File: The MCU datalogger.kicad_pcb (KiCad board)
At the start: 2 copper layers, 25 parts, among them J1 Conn_01x04_Male, J2 Conn_01x09_Male, J3 Conn_01x04_Male, J4 Conn_02x03_Odd_Even, U1 24LC1025, U2 DS1337S+, U3 24LC1025, U4 ATMEGA328P-AU, Y1 32.768 KHz, Y2 16 MHz

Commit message: Setup Pcbnew - imported footprints and updated layout
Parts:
- added H1: MountingHole, MountingHole:MountingHole_2.1mm, F.Cu at (241.0, 46.0)
- added H2: MountingHole, MountingHole:MountingHole_2.1mm, F.Cu at (241.0, 51.8)
- added H3: MountingHole, MountingHole:MountingHole_2.1mm, F.Cu at (241.0, 57.5)
- added H4: MountingHole, MountingHole:MountingHole_2.1mm, F.Cu at (241.0, 63.2)
- added J1: Conn_01x04_Male, Connector_PinHeader_2.54mm:PinHeader_1x04_P2.54mm_Vertical, F.Cu at (213.5, 45.4)
- added J2: Conn_01x09_Male, Connector_PinHeader_2.54mm:PinHeader_1x09_P2.54mm_Vertical, F.Cu at (208.9, 45.4)
- added J3: Conn_01x04_Male, Connector_PinHeader_2.54mm:PinHeader_1x04_P2.54mm_Vertical, F.Cu at (218.1, 45.4)
- added J4: Conn_02x03_Odd_Even, Connector_PinHeader_2.54mm:PinHeader_2x03_P2.54mm_Vertical, F.Cu at (213.5, 57.6)
- added J5: Conn_01x04_Male, Connector_PinHeader_2.54mm:PinHeader_1x04_P2.54mm_Vertical, F.Cu at (229.2, 45.4)
- added J6: Conn_01x09_Male, Connector_PinHeader_2.54mm:PinHeader_1x09_P2.54mm_Vertical, F.Cu at (224.7, 45.4)
- added J7: Conn_01x04_Male, Connector_PinHeader_2.54mm:PinHeader_1x04_P2.54mm_Vertical, F.Cu at (233.8, 45.4)
- added J8: Conn_02x03_Odd_Even, Connector_PinHeader_2.54mm:PinHeader_2x03_P2.54mm_Vertical, F.Cu at (229.2, 57.6)
- moved BT1 85.1 mm to (93.4, 66.2)
- moved C4 85.1 mm to (78.6, 54.7)
- moved D1 85.1 mm to (97.9, 65.4)
- moved D2 85.1 mm to (97.9, 68.4)
- moved J2 85.1 mm to (105.8, 46.4)
- moved R1 85.1 mm to (74.2, 45.6)
- moved R2 85.1 mm to (74.2, 48.6)
- moved R3 85.1 mm to (74.2, 51.5)
- moved R4 85.1 mm to (74.2, 54.5)
- moved R5 85.1 mm to (74.2, 57.4)
- moved R6 85.1 mm to (74.2, 60.4)
- moved R7 85.1 mm to (74.2, 63.3)
- moved U1 85.1 mm to (85.0, 47.5)
- moved U2 85.1 mm to (96.2, 60.6)
- moved Y1 85.1 mm to (86.0, 59.9)
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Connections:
- BT1 pad 1: unconnected-(BT1-+-Pad1) -> Net-(BT1-+)
- BT1 pad 2: unconnected-(BT1---Pad2) -> GND
- C1 pad 1: unconnected-(C1-Pad1) -> Vcc
- C1 pad 2: unconnected-(C1-Pad2) -> GND
- C2 pad 1: unconnected-(C2-Pad1) -> Net-(U4-PB6)
- C2 pad 2: unconnected-(C2-Pad2) -> GND
- C3 pad 1: unconnected-(C3-Pad1) -> Net-(U4-PB7)
- C3 pad 2: unconnected-(C3-Pad2) -> GND
- C4 pad 1: unconnected-(C4-Pad1) -> GND
- C4 pad 2: unconnected-(C4-Pad2) -> Net-(U4-AREF)
- C5 pad 1: unconnected-(C5-Pad1) -> Net-(BT1-+)
- C5 pad 2: unconnected-(C5-Pad2) -> GND
- D1 pad 1: unconnected-(D1-K-Pad1) -> Net-(D1-K)
- D1 pad 2: unconnected-(D1-A-Pad2) -> SCK
- D2 pad 1: unconnected-(D2-K-Pad1) -> Net-(D2-K)
- D2 pad 2: unconnected-(D2-A-Pad2) -> Net-(BT1-+)
- R1 pad 1: unconnected-(R1-Pad1) -> Vcc
- R1 pad 2: unconnected-(R1-Pad2) -> Net-(U2-~{INTA})
- R2 pad 1: unconnected-(R2-Pad1) -> Vcc
- R2 pad 2: unconnected-(R2-Pad2) -> Net-(U2-SQW/~INT)
- R3 pad 1: unconnected-(R3-Pad1) -> Vcc
- R3 pad 2: unconnected-(R3-Pad2) -> SCK
- R4 pad 1: unconnected-(R4-Pad1) -> Vcc
- R4 pad 2: unconnected-(R4-Pad2) -> SDA
- R5 pad 1: unconnected-(R5-Pad1) -> GND
- R5 pad 2: unconnected-(R5-Pad2) -> Net-(D1-K)
- R6 pad 1: unconnected-(R6-Pad1) -> Vcc
- R6 pad 2: unconnected-(R6-Pad2) -> RESET
- R7 pad 1: unconnected-(R7-Pad1) -> Net-(D2-K)
- R7 pad 2: unconnected-(R7-Pad2) -> GND
- U1 pad 1: unconnected-(U1-A0-Pad1) -> Vcc
- U1 pad 2: unconnected-(U1-A1-Pad2) -> Vcc
- U1 pad 3: unconnected-(U1-A2-Pad3) -> Vcc
- U1 pad 4: unconnected-(U1-GND-Pad4) -> GND
- U1 pad 5: unconnected-(U1-SDA-Pad5) -> SDA
- U1 pad 6: unconnected-(U1-SCL-Pad6) -> SCL
- U1 pad 7: unconnected-(U1-WP-Pad7) -> GND
- U1 pad 8: unconnected-(U1-VCC-Pad8) -> Vcc
- U2 pad 1: unconnected-(U2-X1-Pad1) -> Net-(U2-X1)
- U2 pad 2: unconnected-(U2-X2-Pad2) -> Net-(U2-X2)
- U2 pad 3: unconnected-(U2-~{INTA}-Pad3) -> Net-(U2-~{INTA})
- U2 pad 4: unconnected-(U2-GND-Pad4) -> GND
- U2 pad 5: unconnected-(U2-SDA-Pad5) -> SDA
- U2 pad 6: unconnected-(U2-SCL-Pad6) -> SCK
- U2 pad 7: unconnected-(U2-SQW/~INT-Pad7) -> Net-(U2-SQW/~INT)
- U2 pad 8: unconnected-(U2-VCC-Pad8) -> Vcc
- U3 pad 1: unconnected-(U3-A0-Pad1) -> Vcc
- U3 pad 2: unconnected-(U3-A1-Pad2) -> Vcc
- U3 pad 3: unconnected-(U3-A2-Pad3) -> GND
- U3 pad 4: unconnected-(U3-GND-Pad4) -> GND
- U3 pad 5: unconnected-(U3-SDA-Pad5) -> SDA
- U3 pad 6: unconnected-(U3-SCL-Pad6) -> SCK
- U3 pad 7: unconnected-(U3-WP-Pad7) -> GND
- U3 pad 8: unconnected-(U3-VCC-Pad8) -> Vcc
- U4 pad 1: unconnected-(U4-PD3-Pad1) -> D3
- U4 pad 10: unconnected-(U4-PD6-Pad10) -> D6
- U4 pad 11: unconnected-(U4-PD7-Pad11) -> D7
- U4 pad 12: unconnected-(U4-PB0-Pad12) -> D8
- U4 pad 15: unconnected-(U4-PB3-Pad15) -> MOSI
- U4 pad 16: unconnected-(U4-PB4-Pad16) -> MISO
- U4 pad 17: unconnected-(U4-PB5-Pad17) -> SCK
- U4 pad 18: unconnected-(U4-AVCC-Pad18) -> Net-(BT1-+)
- U4 pad 2: unconnected-(U4-PD4-Pad2) -> D4
- U4 pad 20: unconnected-(U4-AREF-Pad20) -> Net-(U4-AREF)
- U4 pad 21: Net-(U4-GND-Pad21) -> GND
- U4 pad 27: unconnected-(U4-PC4-Pad27) -> SDA
- U4 pad 28: unconnected-(U4-PC5-Pad28) -> SCK
- U4 pad 29: unconnected-(U4-PC6/~{RESET}-Pad29) -> RESET
- U4 pad 3: Net-(U4-GND-Pad21) -> GND
- U4 pad 30: unconnected-(U4-PD0-Pad30) -> RX
- U4 pad 31: unconnected-(U4-PD1-Pad31) -> TX
- U4 pad 32: unconnected-(U4-PD2-Pad32) -> D2
- U4 pad 4: Net-(U4-VCC-Pad4) -> Net-(BT1-+)
- U4 pad 5: Net-(U4-GND-Pad21) -> GND
- U4 pad 6: Net-(U4-VCC-Pad4) -> unconnected-(U4-VCC-Pad6)
- U4 pad 7: unconnected-(U4-PB6-Pad7) -> Net-(U4-PB6)
- U4 pad 8: unconnected-(U4-PB7-Pad8) -> Net-(U4-PB7)
- U4 pad 9: unconnected-(U4-PD5-Pad9) -> D5
- Y1 pad 1: unconnected-(Y1-Pad1) -> Net-(U2-X2)
- Y1 pad 2: unconnected-(Y1-Pad2) -> Net-(U2-X1)
- Y2 pad 1: unconnected-(Y2-Pad1) -> Net-(U4-PB7)
- Y2 pad 2: unconnected-(Y2-Pad2) -> Net-(U4-PB6)

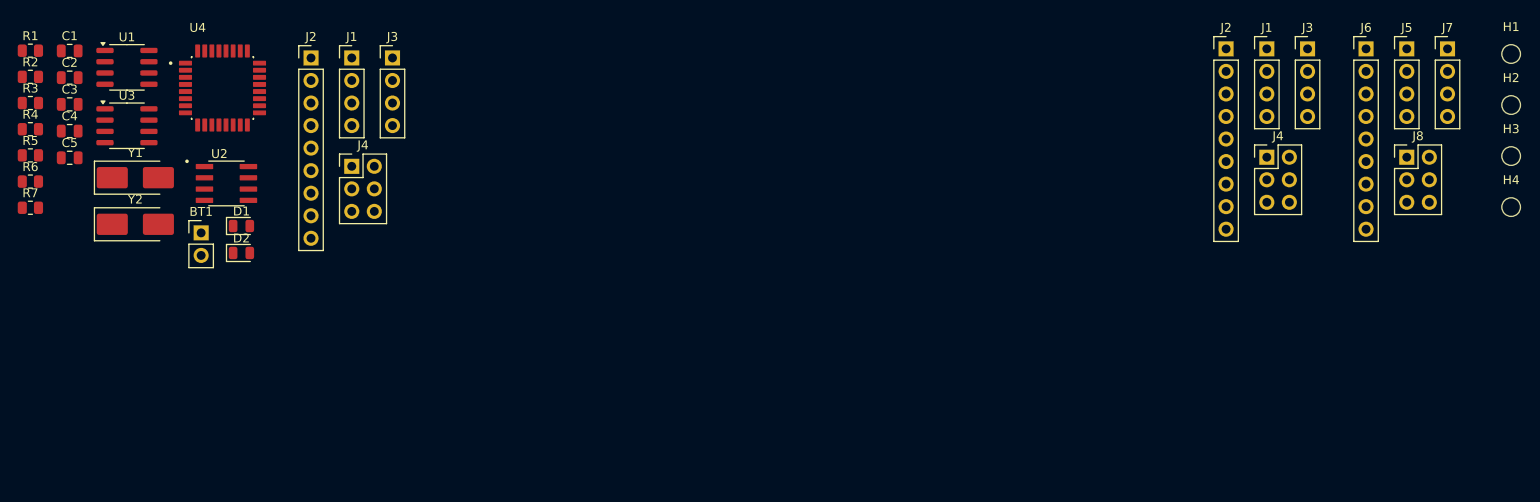
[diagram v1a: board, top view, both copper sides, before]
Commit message: Completed placement of footprints.
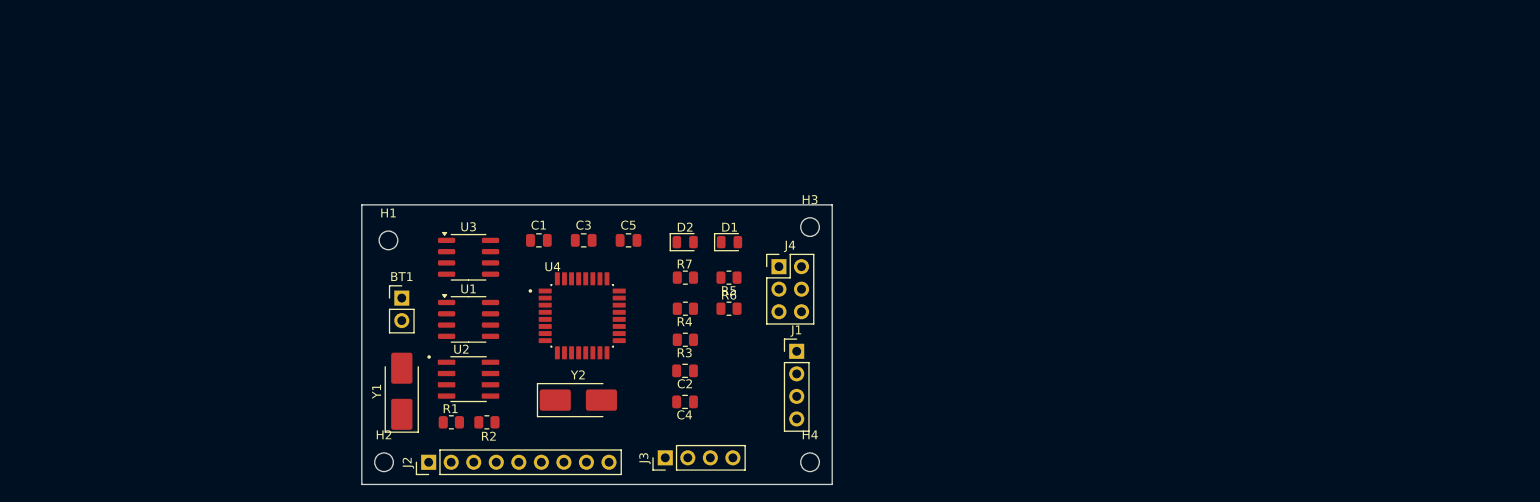
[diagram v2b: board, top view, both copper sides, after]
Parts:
- removed the J1 at (110.4, 46.4)
- removed the J2 at (105.8, 46.4)
- removed the J3 at (115.0, 46.4)
- removed the J4 at (110.4, 58.7)
- removed J5, J7: Conn_01x04_Male, Connector_PinHeader_2.54mm:PinHeader_1x04_P2.54mm_Vertical
- removed J6: Conn_01x09_Male, Connector_PinHeader_2.54mm:PinHeader_1x09_P2.54mm_Vertical
- removed J8: Conn_02x03_Odd_Even, Connector_PinHeader_2.54mm:PinHeader_2x03_P2.54mm_Vertical
- moved H2 133.2 mm to (114.0, 92.0)
- moved H1 128.2 mm to (114.5, 67.0)
- moved J2 101.2 mm to (119.0, 92.0), turned to 90 degrees
- moved J3 85.8 mm to (145.7, 91.5), turned to 90 degrees
- moved H4 84.1 mm to (162.0, 92.0)
- moved R6 80.0 mm to (152.9, 74.7)
- moved R5 79.9 mm to (152.9, 71.2), turned to 180 degrees
- moved H3 79.4 mm to (162.0, 65.5)
- moved R3 78.5 mm to (148.0, 78.2)
- moved C2 76.8 mm to (147.9, 81.7)
- moved R4 76.5 mm to (148.0, 74.7)
- moved C4 75.8 mm to (147.9, 85.2)
- moved R7 74.2 mm to (148.0, 71.2)
- moved R2 64.5 mm to (125.6, 87.5)
- moved C5 63.6 mm to (141.6, 67.0)
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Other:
- board outline added: 53 x 31.5 mm
